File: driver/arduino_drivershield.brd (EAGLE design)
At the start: 59.7 x 54.3 mm, 37 parts, among them IC1 LB1973M, IC10 LB1973M, IC11 LB1973M, IC12 74HC14D, IC2 LB1973M, IC3 74HC14D, IC4 LB1973M, IC5 LB1973M, IC6 74HC14D, IC7 LB1973M, IC8 LB1973M, IC9 74HC14D, U1 ARDUINO_SHIELDLABEL

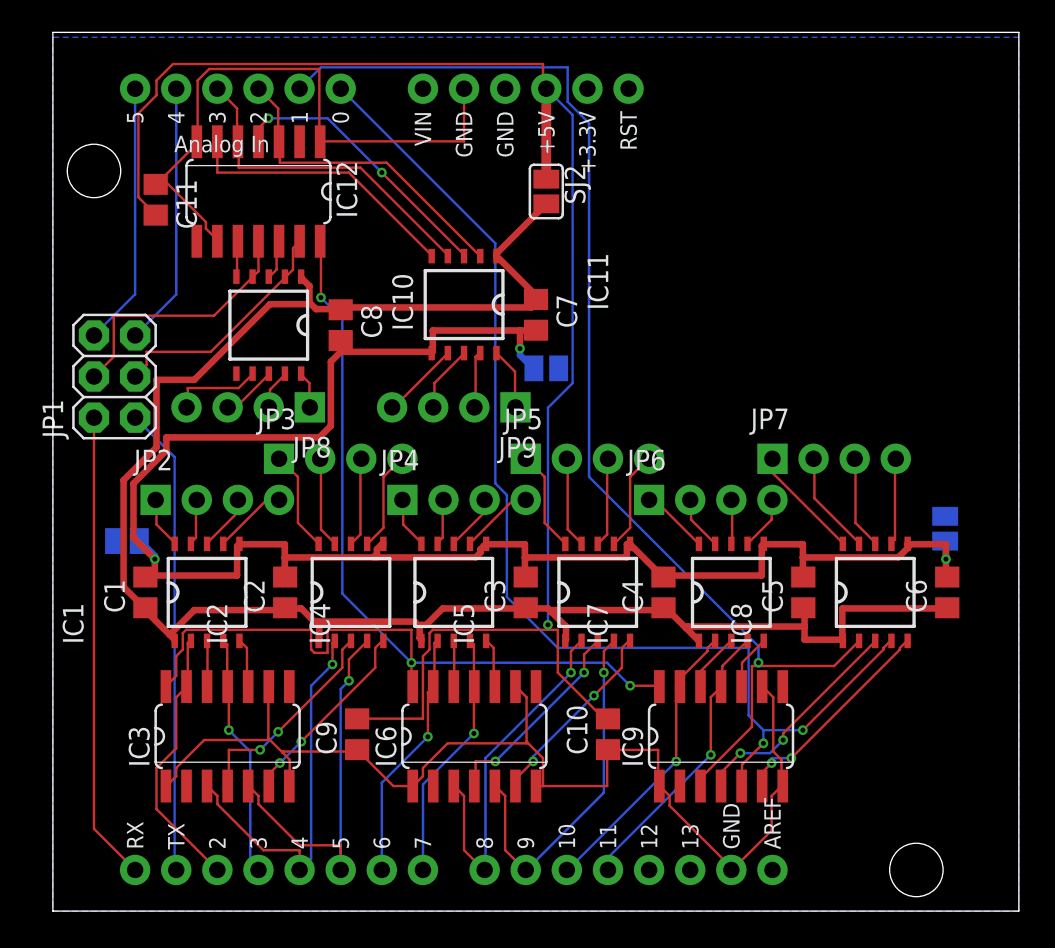
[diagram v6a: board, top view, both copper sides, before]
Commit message: tuning dimension to the shield outline
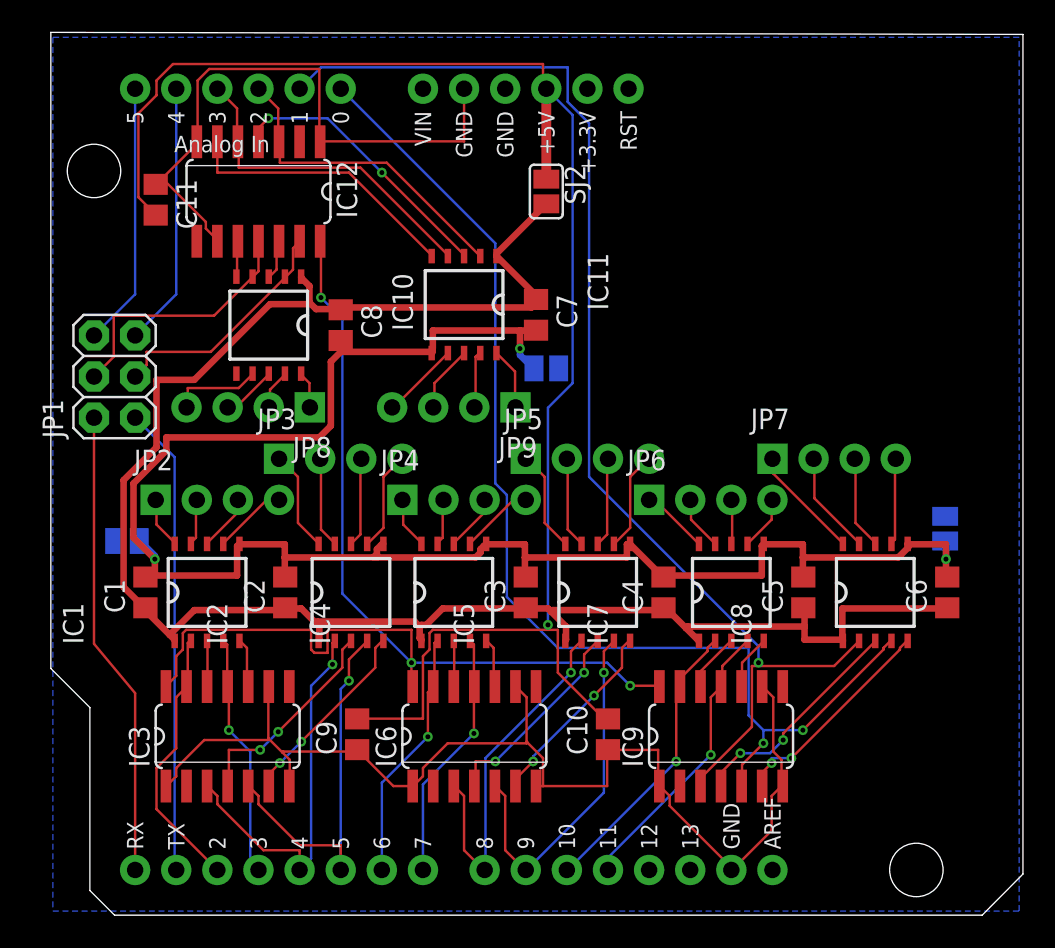
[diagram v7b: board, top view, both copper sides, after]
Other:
- board size 59.7 x 54.3 mm -> 60.1 x 54.5 mm
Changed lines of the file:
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@@
 <setting verticaltext="up"/>
 </settings>
-<grid distance="10" unitdist="mil" unit="mil" style="lines" multiple="1" display="yes" altdistance="0.025" altunitdist="inch" altunit="mil"/>
+<grid distance="5" unitdist="mil" unit="mil" style="lines" multiple="1" display="yes" altdistance="0.025" altunitdist="inch" altunit="mil"/>
 <layers>
 <layer number="1" name="Top" color="4" fill="1" visible="yes" active="yes"/>
@@
 <board>
 <plain>
-<wire x1="0" y1="0" x2="59.67" y2="0" width="0" layer="20"/>
-<wire x1="59.67" y1="0" x2="59.67" y2="54.28" width="0" layer="20"/>
-<wire x1="59.67" y1="54.28" x2="0" y2="54.28" width="0" layer="20"/>
-<wire x1="0" y1="54.28" x2="0" y2="0" width="0" layer="20"/>
+<wire x1="3.81" y1="-0.254" x2="57.404" y2="-0.254" width="0" layer="20"/>
+<wire x1="57.404" y1="-0.254" x2="59.924" y2="2.286" width="0" layer="20"/>
+<wire x1="59.924" y1="2.286" x2="59.924" y2="54.153" width="0" layer="20"/>
+<wire x1="59.924" y1="54.153" x2="-0.127" y2="54.28" width="0" layer="20"/>
+<wire x1="-0.127" y1="54.28" x2="-0.127" y2="14.986" width="0" layer="20"/>
+<wire x1="-0.127" y1="14.986" x2="2.286" y2="12.573" width="0" layer="20"/>
+<wire x1="2.286" y1="12.573" x2="2.286" y2="1.27" width="0" layer="20"/>
+<wire x1="2.286" y1="1.27" x2="3.81" y2="-0.254" width="0" layer="20"/>
 </plain>
 <attributes>
@@
 <contactref element="U1" pad="RX"/>
 <contactref element="JP1" pad="2"/>
-<wire x1="2.54" y1="5.08" x2="5.08" y2="2.54" width="0.1524" layer="1"/>
-<wire x1="2.54" y1="30.48" x2="2.54" y2="5.08" width="0.1524" layer="1"/>
+<wire x1="5.08" y1="13.462" x2="5.08" y2="2.54" width="0.1524" layer="1"/>
+<wire x1="2.54" y1="30.48" x2="2.54" y2="16.51" width="0.1524" layer="1"/>
+<wire x1="2.54" y1="16.51" x2="5.08" y2="13.462" width="0.1524" layer="1"/>
 </signal>
 <signal name="TX">

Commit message: dimension should be nicer now
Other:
- board size 60.1 x 54.5 mm -> 60 x 53.7 mm
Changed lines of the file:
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@@
 <board>
 <plain>
-<wire x1="3.81" y1="-0.254" x2="57.404" y2="-0.254" width="0" layer="20"/>
-<wire x1="57.404" y1="-0.254" x2="59.924" y2="2.286" width="0" layer="20"/>
-<wire x1="59.924" y1="2.286" x2="59.924" y2="54.153" width="0" layer="20"/>
-<wire x1="59.924" y1="54.153" x2="-0.127" y2="54.28" width="0" layer="20"/>
-<wire x1="-0.127" y1="54.28" x2="-0.127" y2="14.986" width="0" layer="20"/>
+<wire x1="3.7592" y1="-0.2032" x2="57.2262" y2="-0.2032" width="0" layer="20"/>
+<wire x1="57.2262" y1="-0.2032" x2="59.8986" y2="2.4638" width="0" layer="20"/>
+<wire x1="59.8986" y1="2.4638" x2="59.8932" y2="50.8508" width="0" layer="20"/>
+<wire x1="59.8932" y1="50.8508" x2="57.277" y2="53.467" width="0" layer="20"/>
+<wire x1="57.277" y1="53.467" x2="2.393" y2="53.4926" width="0" layer="20"/>
+<wire x1="2.393" y1="53.4926" x2="2.3876" y2="50.9524" width="0" layer="20"/>
+<wire x1="2.3876" y1="50.9524" x2="-0.127" y2="48.438" width="0" layer="20"/>
+<wire x1="-0.127" y1="48.438" x2="-0.127" y2="14.986" width="0" layer="20"/>
 <wire x1="-0.127" y1="14.986" x2="2.286" y2="12.573" width="0" layer="20"/>
 <wire x1="2.286" y1="12.573" x2="2.286" y2="1.27" width="0" layer="20"/>
-<wire x1="2.286" y1="1.27" x2="3.81" y2="-0.254" width="0" layer="20"/>
+<wire x1="2.286" y1="1.27" x2="3.7592" y2="-0.2032" width="0" layer="20"/>
 </plain>
 <attributes>
